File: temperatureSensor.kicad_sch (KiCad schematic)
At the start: 4 parts, among them IC1 LMT87LPG

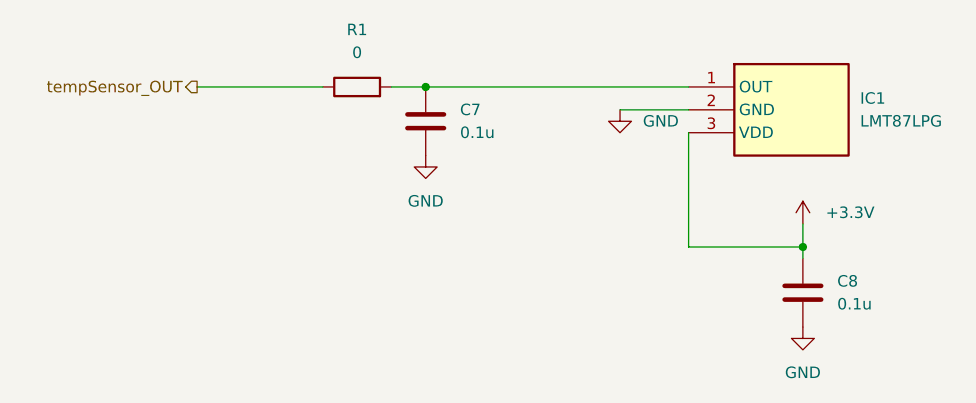
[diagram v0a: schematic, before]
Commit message: assigned footprints for all capacitors
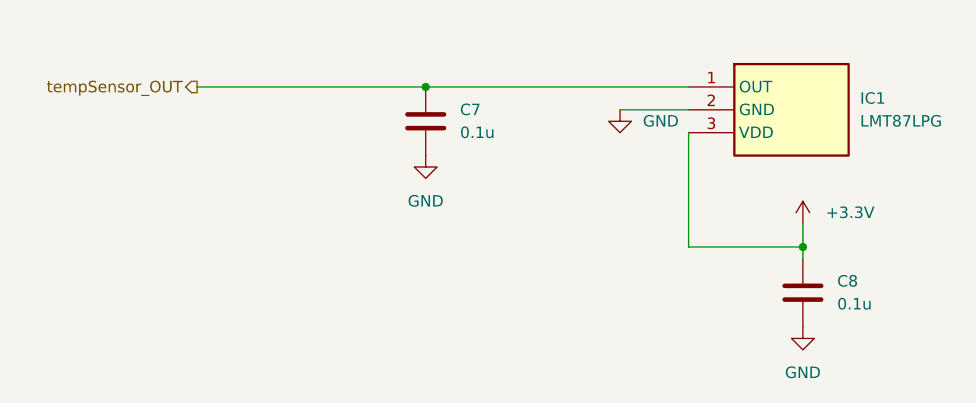
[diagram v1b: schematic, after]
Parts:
- removed R1: 0, symbol Device:R
- C7, C8: footprint (none) -> Capacitor_SMD:C_0805_2012Metric
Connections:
- net tempSensor_OUT: now also C7.1, IC1.1 (OUT)
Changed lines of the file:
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@@
   (junction (at 110.49 92.71) (diameter 0) (color 0 0 0 0)
-  )
-  (wire (pts (xy 43.18 74.93) (xy 57.15 74.93))
-    (stroke (width 0) (type default))
   )
   (wire (pts (xy 110.49 92.71) (xy 110.49 93.98))
@@
     (stroke (width 0) (type default))
   )
-  (wire (pts (xy 64.77 74.93) (xy 68.58 74.93))
+  (wire (pts (xy 43.18 74.93) (xy 68.58 74.93))
     (stroke (width 0) (type default))
   )
   (hierarchical_label "tempSensor_OUT" (shape output) (at 43.18 74.93 180) (fields_autoplaced)
     (effects (font (size 1.27 1.27)) (justify right))
-  )
-  (symbol (lib_id "Device:R") (at 60.96 74.93 90) (unit 1)
-    (in_bom yes) (on_board yes) (dnp no) (fields_autoplaced)
-    (property "Reference" "R1" (at 60.96 68.58 90)
-      (effects (font (size 1.27 1.27)))
-    )
-    (property "Value" "0" (at 60.96 71.12 90)
-      (effects (font (size 1.27 1.27)))
-    )
-    (property "Footprint" "" (at 60.96 76.708 90)
-      (effects (font (size 1.27 1.27)) hide)
-    )
-    (property "Datasheet" "~" (at 60.96 74.93 0)
-      (effects (font (size 1.27 1.27)) hide)
-    )
-    (pin "1")
-    (pin "2")
-    (instances
-      (project "Telemetry-Peripheral-SOM-Daughterboard-IMU"
-        (path "/637f68f0-cb9c-412a-8573-5d8e7ef6d8a2/0366cb5e-31c7-40b1-9d0c-97ad688b48f0"
-          (reference "R1") (unit 1)
-        )
-      )
-    )
   )
   (symbol (lib_id "Device:C") (at 110.49 97.79 0) (unit 1)
@@
       (effects (font (size 1.27 1.27)) (justify left))
     )
-    (property "Footprint" "" (at 111.4552 101.6 0)
+    (property "Footprint" "Capacitor_SMD:C_0805_2012Metric" (at 111.4552 101.6 0)
       (effects (font (size 1.27 1.27)) hide)
     )
@@
       (effects (font (size 1.27 1.27)) (justify left))
     )
-    (property "Footprint" "" (at 69.5452 82.55 0)
+    (property "Footprint" "Capacitor_SMD:C_0805_2012Metric" (at 69.5452 82.55 0)
       (effects (font (size 1.27 1.27)) hide)
     )

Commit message: fixed spi1_nss conflict, switched imu to spi2
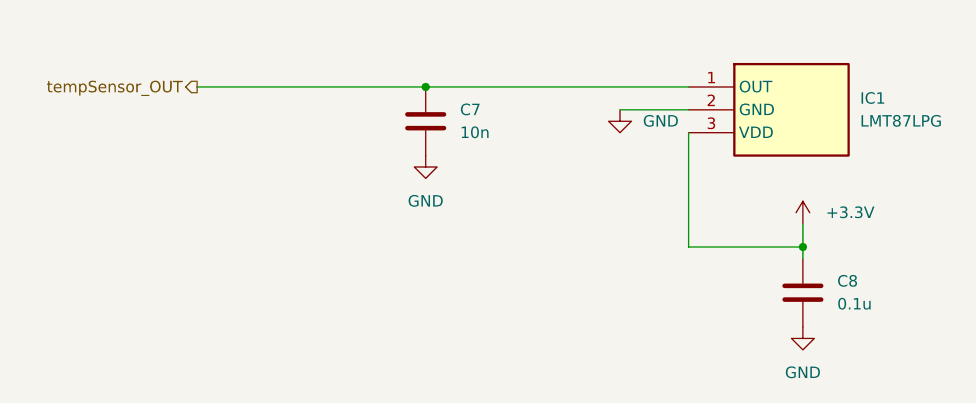
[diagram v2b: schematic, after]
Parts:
- C7: value 0.1u -> 10n
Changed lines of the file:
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@@
       (effects (font (size 1.27 1.27)) (justify left))
     )
-    (property "Value" "0.1u" (at 72.39 80.01 0)
+    (property "Value" "10n" (at 72.39 80.01 0)
       (effects (font (size 1.27 1.27)) (justify left))
     )
